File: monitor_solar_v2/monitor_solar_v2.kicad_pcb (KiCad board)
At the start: 2 copper layers, 66 x 45 mm, 25 parts, among them J1 Screw_Terminal_01x02, J2 Conn_01x03_Socket, J3 Screw_Terminal_01x02, J4 Conn_01x04_Pin, J5 Conn_01x03_Pin, U1 X9C103S, U2 AMS1117-3.3, U4 LM358

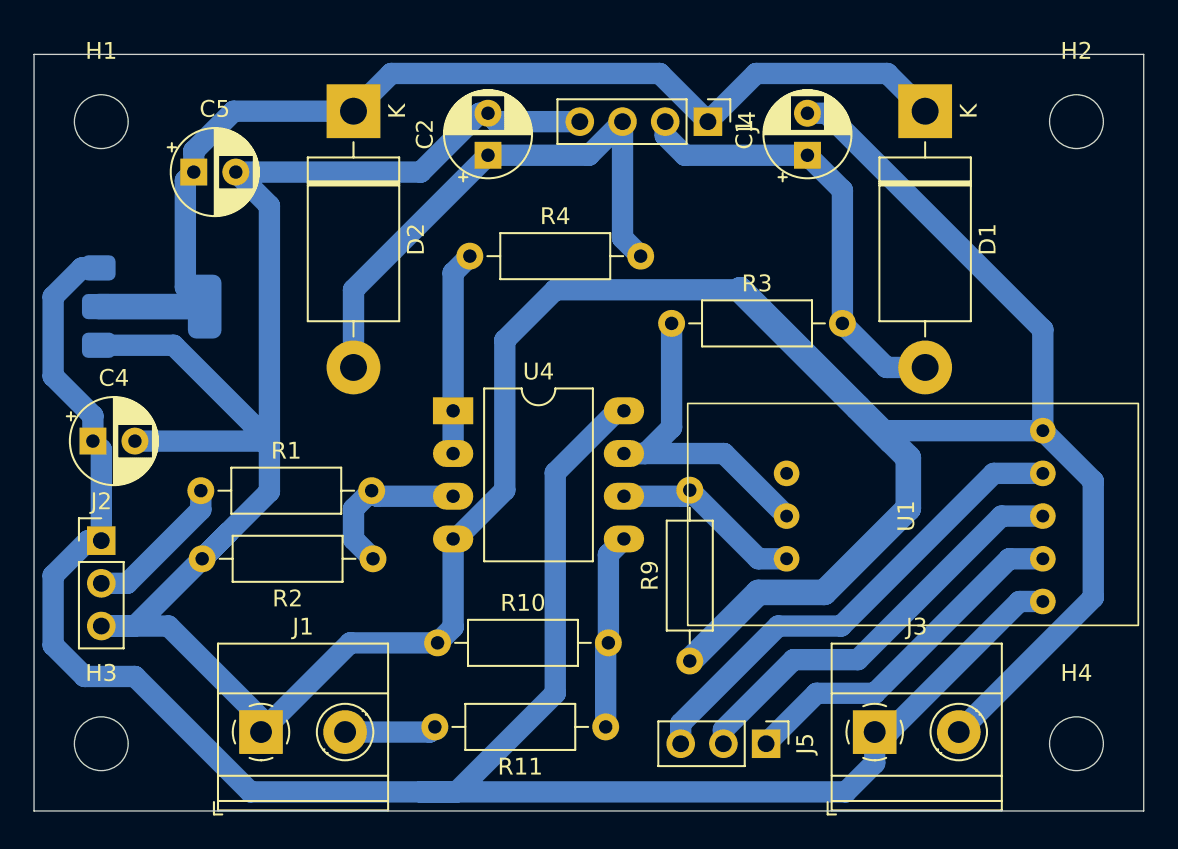
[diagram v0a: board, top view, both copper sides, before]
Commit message: Test Flatcam
Prueba para utilizar flatcam a partir de la pcb v2
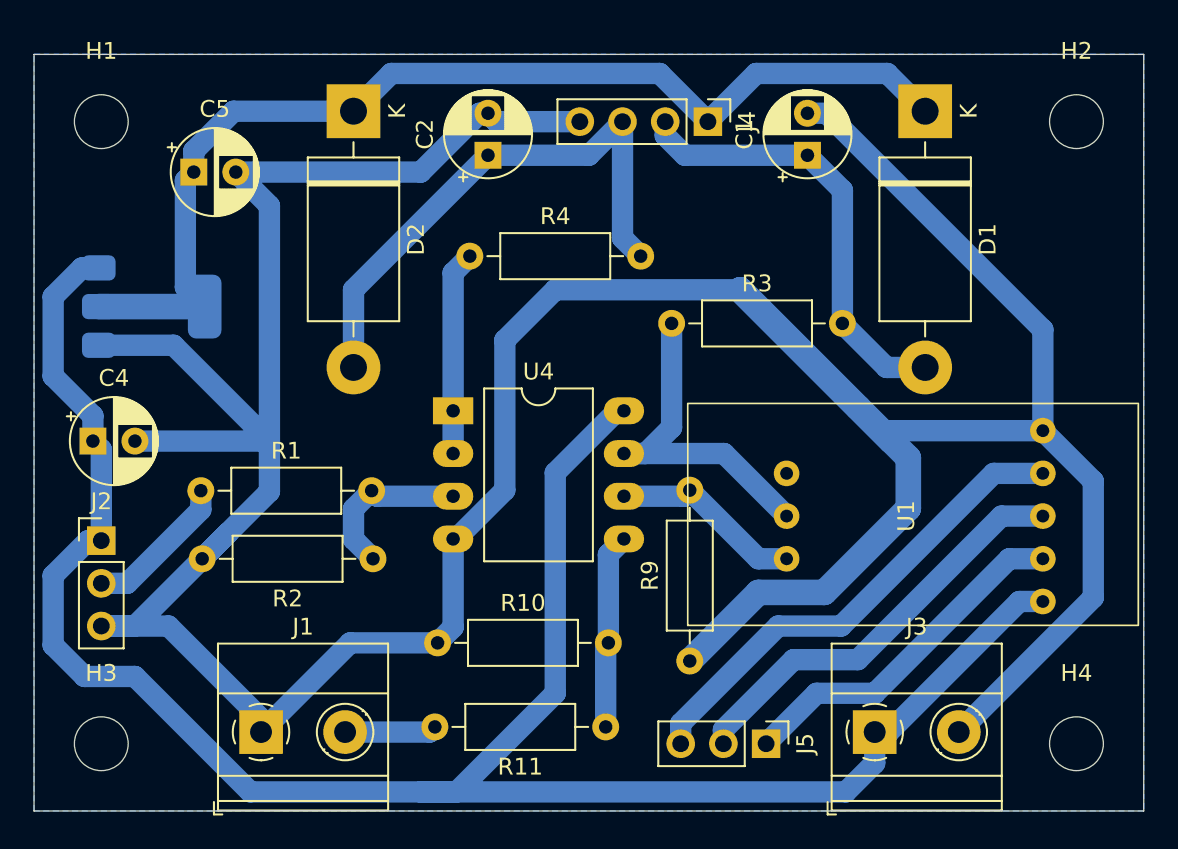
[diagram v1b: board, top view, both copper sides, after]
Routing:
- added copper zone on B.Cu, net GND

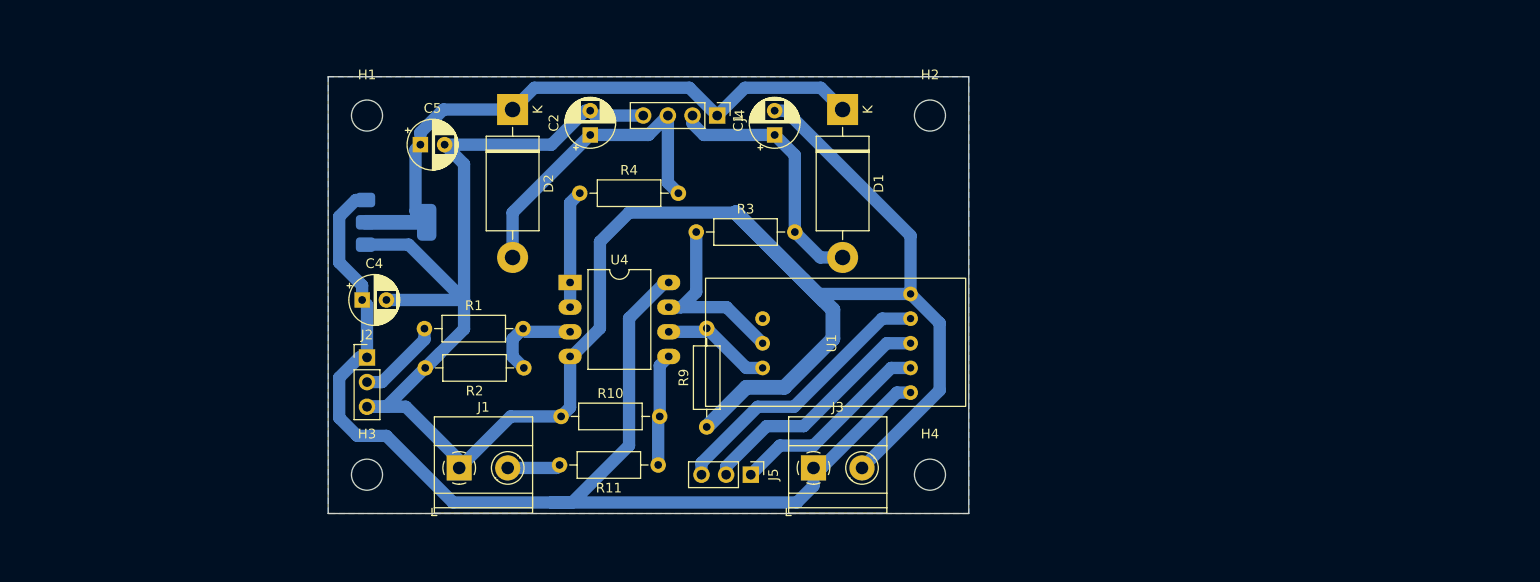
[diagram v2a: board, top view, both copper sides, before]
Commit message: Adding ESP-12 and new pcb
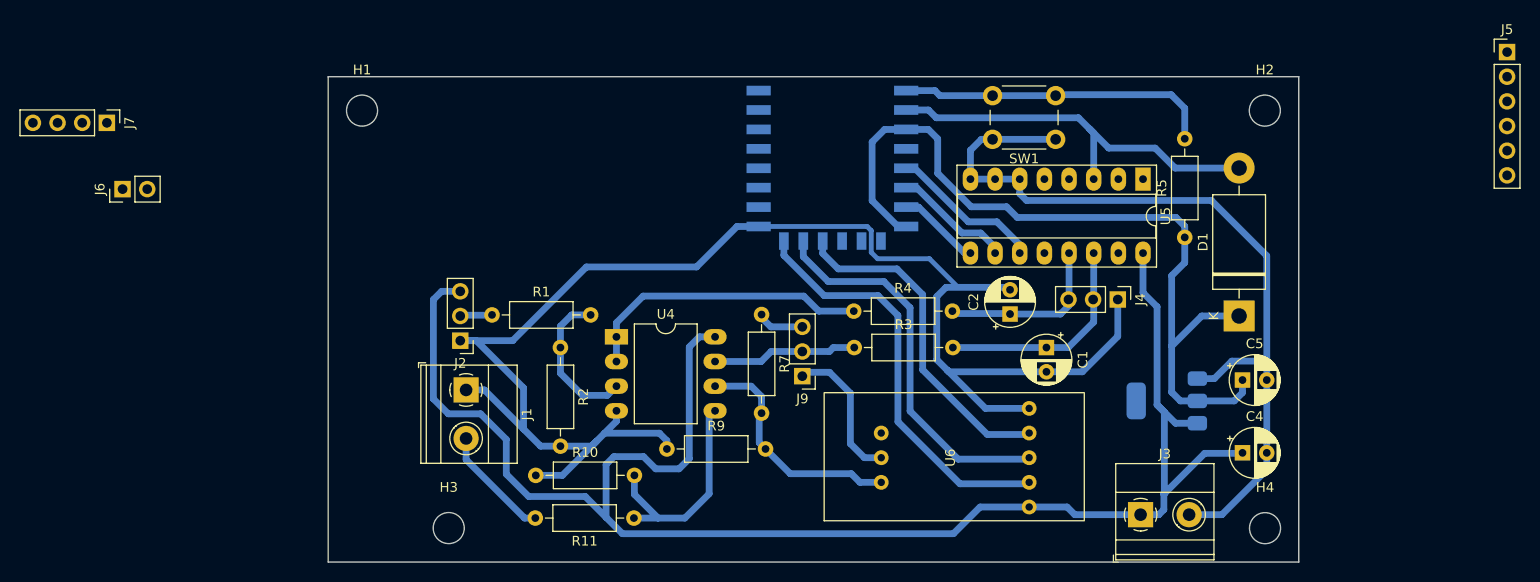
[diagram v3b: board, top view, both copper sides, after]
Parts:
- removed D2: 1N5822, Diode_THT:D_DO-201AD_P15.24mm_Horizontal
- removed U1: X9C103S, RF_GPS:X9C103S
- added J6: JUMPER_PROG, Connector_PinHeader_2.54mm:PinHeader_1x02_P2.54mm_Vertical, F.Cu at (-1.18, 31.6)
- added J7: PROGRAM, Connector_PinHeader_2.54mm:PinHeader_1x04_P2.54mm_Vertical, F.Cu at (-2.80, 24.8)
- added J9: Jumper_fixed_r, Connector_PinHeader_2.54mm:PinHeader_1x03_P2.54mm_Vertical, F.Cu at (68.8, 50.9)
- added R5: 10k, Resistor_THT:R_Axial_DIN0207_L6.3mm_D2.5mm_P10.16mm_Horizontal, F.Cu at (108.2, 36.5)
- added R7: 3.3k, Resistor_THT:R_Axial_DIN0207_L6.3mm_D2.5mm_P10.16mm_Horizontal, F.Cu at (64.7, 44.5)
- added SW1: SW_Push, Button_Switch_THT:SW_PUSH_6mm, F.Cu at (95.0, 26.4)
- added U3: ESP-12F, RF_Module:ESP-12E, B.Cu at (72.0, 24.9)
- added U5: 4051, Package_DIP:DIP-16_W7.62mm_Socket_LongPads, F.Cu at (104.0, 30.6)
- added U6: X9C103S, Componentes:X9C103S, F.Cu at (84.6, 59.2)
- J1: value Screw_Terminal_01x02 -> Panel
- J2: value Conn_01x03_Socket -> ACS712
- J3: value Screw_Terminal_01x02 -> Reg 5V
- J4: value Conn_01x04_Pin -> AMP_OUT; footprint Connector_PinHeader_2.54mm:PinHeader_1x04_P2.54mm_Vertical -> Connector_PinHeader_2.54mm:PinHeader_1x03_P2.54mm_Vertical
- J5: value Conn_01x03_Pin -> GPIO; footprint Connector_PinHeader_2.54mm:PinHeader_1x03_P2.54mm_Vertical -> Connector_PinHeader_2.54mm:PinHeader_1x06_P2.54mm_Vertical
- R1: value 22k -> 20k
- moved C4 92.1 mm to (114.2, 58.8)
- moved J5 89.3 mm to (141.5, 17.5), turned to 0 degrees
- moved C5 88.1 mm to (114.2, 51.2)
- moved U2 81.5 mm to (106.4, 53.4), turned to 180 degrees
- moved C2 47.0 mm to (90.2, 44.5)
- moved D1 46.1 mm to (113.8, 44.6), turned to 90 degrees
- moved J4 45.4 mm to (101.3, 43.0)
- moved C1 35.5 mm to (94.0, 47.9), turned to -90 degrees
- moved H4 35.0 mm to (116.5, 66.5)
- moved H2 34.5 mm to (116.5, 23.5)
- moved J3 34.0 mm to (103.7, 65.1)
- moved R4 30.7 mm to (74.2, 44.1)
- moved R3 20.2 mm to (74.2, 47.9)
- moved H3 10.1 mm to (32.4, 66.5)
- moved J2 9.76 mm to (33.6, 47.2), turned to 180 degrees
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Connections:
- net Pot+ renamed Net-(J9-Pin_2)
- C1 pad 1: Net-(D1-A) -> Vamp2
- C2 pad 1: Net-(D2-A) -> Vamp1
- D1 pad 2: Net-(D1-A) -> ADC_IN
- J2 pad 1: +5V -> GND
- J2 pad 3: GND -> +5V
- J4 pad 1: +3.3V -> GND
- J4 pad 2: Net-(D1-A) -> Vamp2
- J4 pad 3: Net-(D2-A) -> Vamp1
- J5 pad 1: POT_CS -> unconnected-(J5-Pin_1-Pad1)
- J5 pad 2: STEP -> unconnected-(J5-Pin_2-Pad2)
- J5 pad 3: DIR -> unconnected-(J5-Pin_3-Pad3)
- R3 pad 2: Net-(D1-A) -> Vamp2
- R4 pad 1: Vamp1 -> Net-(U4A--)
- R4 pad 2: Net-(D2-A) -> Vamp1
- U4 pad 1: Vamp1 -> Net-(U4A--)
- U4 pad 2: Vamp1 -> Net-(U4A--)
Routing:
- net +5V: track 124.4 -> 170.2 mm
- net ADC_IN: track 0.00 -> 42.1 mm
- net Net-(D2-A): track 33.2 -> 0.00 mm
- net Net-(U3-~{RST}): track 0.00 -> 32.7 mm
- net Net-(U4A--): track 0.00 -> 30.2 mm
- net Net-(D1-A): track 26.6 -> 0.00 mm
- net Vamp2: track 0.00 -> 22.7 mm
- net POT_CS: track 21.0 -> 43.0 mm
- net +3.3V: track 64.9 -> 84.8 mm
- net MUX_A: track 0.00 -> 15.8 mm
- net Pot+: track 0.00 -> 15.0 mm
- net STEP: track 25.1 -> 39.8 mm
- net Pot-: track 11.5 -> 24.3 mm
- net MUX_B: track 0.00 -> 12.3 mm
- net Net-(U4B-+): track 11.6 -> 22.9 mm
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- removed copper zone on B.Cu, net GND
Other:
- board size 66 x 45 mm -> 100 x 50 mm

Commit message: PCB esp12 v1.0
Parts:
- added G***: LOGO, LOGO, B.Cu at (31.8, 32.3)
- added J8: GPIO_2, Connector_PinHeader_2.54mm:PinHeader_1x02_P2.54mm_Vertical, F.Cu at (65.5, 48.4)
- added R6: 10k, Resistor_THT:R_Axial_DIN0207_L6.3mm_D2.5mm_P10.16mm_Horizontal, F.Cu at (80.1, 43.5)
- J1: footprint TerminalBlock_Phoenix:TerminalBlock_Phoenix_MKDS-1,5-2_1x02_P5.00mm_Horizontal -> TerminalBlock_Phoenix:TerminalBlock_Phoenix_MKDS-1,5-2-5.08_1x02_P5.08mm_Horizontal
- J5: value GPIO -> JUMPER_PROG; footprint Connector_PinHeader_2.54mm:PinHeader_1x06_P2.54mm_Vertical -> Connector_PinHeader_2.54mm:PinHeader_1x02_P2.54mm_Vertical
- moved J5 91.3 mm to (53.3, 41.4), turned to 180 degrees
- moved J7 57.8 mm to (55.0, 24.0)
- moved J6 42.5 mm to (40.6, 24.0)
- moved R7 10.2 mm to (61.4, 54.1)
- moved J9 9.84 mm to (65.5, 60.1)
- moved J2 9.61 mm to (24.1, 48.5)
- moved J1 9.48 mm to (24.9, 53.8)
- moved R9 9.05 mm to (45.9, 59.3)
- moved R2 8.93 mm to (36.2, 52.5)
- moved U3 8.86 mm to (68.3, 33.0)
- moved H3 8.33 mm to (24.1, 66.2)
- moved R1 7.86 mm to (30.1, 48.6)
- moved R3 7.23 mm to (75.3, 55.0)
- moved R10 6.99 mm to (48.2, 62.6)
- moved R4 6.74 mm to (75.3, 50.8)
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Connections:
- J4 pad 1: GND -> Vamp2
- J4 pad 2: Vamp2 -> GND
- J5 pad 1: unconnected-(J5-Pin_1-Pad1) -> GPIO15
- J5 pad 2: unconnected-(J5-Pin_2-Pad2) -> GPIO2
- U3 pad 10: unconnected-(U3-MISO-Pad10) -> DIR
- U3 pad 11: unconnected-(U3-GPIO9-Pad11) -> STEP
- U3 pad 12: DIR -> POT_CS
- U3 pad 13: STEP -> Net-(J8-Pin_1)
- U3 pad 14: POT_CS -> Net-(J8-Pin_2)
- U3 pad 16: unconnected-(U3-GPIO15-Pad16) -> GPIO15
- U3 pad 17: unconnected-(U3-GPIO2-Pad17) -> GPIO2
- U3 pad 20: unconnected-(U3-GPIO5-Pad20) -> +3.3V
- U3 pad 3: +3.3V -> Net-(U3-EN)
- U3 pad 4: unconnected-(U3-GPIO16-Pad4) -> +3.3V
- U3 pad 5: MUX_A -> MUX_B
- U3 pad 6: MUX_B -> MUX_C
- U3 pad 7: MUX_C -> MUX_A
- U3 pad 9: unconnected-(U3-CS0-Pad9) -> GND
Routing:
- net GND: track 245.0 -> 394.2 mm
- net +3.3V: track 84.8 -> 118.6 mm
- net Net-(J6-Pin_2): track 0.00 -> 23.6 mm
- net RX: track 0.00 -> 13.6 mm
- net Pot-: track 24.3 -> 35.9 mm
- net Net-(J9-Pin_2): track 14.9 -> 24.9 mm
- net TX: track 0.00 -> 9.85 mm
- net Vpanel: track 11.8 -> 20.4 mm
- net GPIO2: track 0.00 -> 7.74 mm
- net Vamp2: track 22.7 -> 30.4 mm
- net GPIO15: track 0.00 -> 7.51 mm
- net ADC_IN: track 42.1 -> 49.2 mm
- net POT_CS: track 43.0 -> 36.6 mm
- net Net-(U4B-+): track 22.9 -> 16.8 mm
- net Net-(U4A--): track 30.2 -> 36.3 mm
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- added copper zone on B.Cu, net GND
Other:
- board text added: "Pablo Gomez 2025"

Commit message: codigo v1: pruebas en telegram
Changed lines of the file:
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@@
 	)
 	(segment
-		(start 68.5 60.125)
-		(end 70.475 62.1)
+		(start 71.8 62.1)
+		(end 75.88 62.1)
+		(width 0.7)
+		(layer "B.Cu")
+		(net 12)
+	)
+	(segment
+		(start 69.825 60.125)
+		(end 71.8 62.1)
 		(width 0.7)
 		(layer "B.Cu")
@@
 	(segment
 		(start 65.55 60.125)
-		(end 68.5 60.125)
-		(width 0.7)
-		(layer "B.Cu")
-		(net 12)
-	)
-	(segment
-		(start 70.475 62.1)
-		(end 75.88 62.1)
+		(end 69.825 60.125)
 		(width 0.7)
 		(layer "B.Cu")
@@
 	)
 	(segment
-		(start 65.55 57.585)
-		(end 70.94 57.585)
-		(width 0.7)
-		(layer "B.Cu")
-		(net 31)
-	)
-	(segment
 		(start 55.115 50.59)
 		(end 62.11 57.585)
@@
 	)
 	(segment
+		(start 69.915 57.585)
+		(end 72.45 55.05)
+		(width 0.7)
+		(layer "B.Cu")
+		(net 31)
+	)
+	(segment
 		(start 62.11 57.585)
 		(end 65.55 57.585)
@@
 	)
 	(segment
-		(start 70.94 57.585)
-		(end 73.475 55.05)
+		(start 72.45 55.05)
+		(end 75.3 55.05)
 		(width 0.7)
 		(layer "B.Cu")
@@
 	)
 	(segment
-		(start 73.475 55.05)
-		(end 75.3 55.05)
-		(width 0.7)
-		(layer "B.Cu")
+		(start 65.55 57.585)
+		(end 69.915 57.585)
+		(width 0.7)
+		(layer "B.Cu")
